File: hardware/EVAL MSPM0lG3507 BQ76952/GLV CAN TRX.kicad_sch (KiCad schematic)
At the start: 18 parts, among them Q2 2N7002, U10 MCP2542FDxMF, U5 ISO7721D, U9 LMR51603XDBVR

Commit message: boards finalized
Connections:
- net -GLV: now also C10.2, C22.2, C35.2, D11.1 (K), Q2.2 (S), R39.1, U9.2 (GND)
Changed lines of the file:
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@@
+	)
+	(junction
+		(at 127 48.26)
+		(diameter 0)
+		(color 0 0 0 0)
 	)
 	(junction
@@
 		(pts
 			(xy 69.85 91.44) (xy 69.85 93.98)
+		)
+		(stroke
+			(width 0)
+			(type default)
+		)
+	)
+	(wire
+		(pts
+			(xy 127 48.26) (xy 138.43 48.26)
 		)
 		(stroke
@@
 		(effects
 			(font
+				(size 1.27 1.27)
+			)
+			(justify left bottom)
+		)
+	)
+	(label "-GLV"
+		(at 138.43 48.26 0)
+		(effects
+			(font

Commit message: partial correctinos to kicad
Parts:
- D11: footprint LED_SMD:LED_0201_0603Metric_Pad0.64x0.40mm_HandSolder -> LED_SMD:LED_0603_1608Metric; unit x10 0.12 -> 0.118
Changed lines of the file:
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@@
 			)
 		)
-		(property "Footprint" "LED_SMD:LED_0201_0603Metric_Pad0.64x0.40mm_HandSolder"
+		(property "Footprint" "LED_SMD:LED_0603_1608Metric"
 			(at 127 34.29 0)
 			(effects
@@
 			)
 		)
-		(property "unit x10" "0.12"
+		(property "unit x10" "0.118"
 			(at 127 34.29 90)
 			(effects

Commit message: asdd
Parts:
- L4: mouser (none) -> https://www.mouser.com/ProductDetail/Bourns/SRN5040TA-101K?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; specs (none) -> 100uH, 10%, 720mA max, 560mESR, -55C, +125C; unit x10 (none) -> 0.329
- R31: value 700 -> 750; mouser (none) -> https://www.mouser.com/ProductDetail/YAGEO/RC1206JR-13750RL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; specs (none) -> 750mOhm, 250mW, 5%, 100PPM, 200C, -55C, +155C; unit x10 (none) -> 0.022
- U10: mouser (none) -> https://www.mouser.com/ProductDetail/579-MCP2542FD-E-SN; unit x10 (none) -> 0.86
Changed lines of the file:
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@@
 	(wire
 		(pts
-			(xy 53.34 76.2) (xy 53.34 93.98)
+			(xy 50.8 76.2) (xy 50.8 93.98)
 		)
 		(stroke
@@
 	(wire
 		(pts
+			(xy 50.8 76.2) (xy 48.26 76.2)
+		)
+		(stroke
+			(width 0)
+			(type default)
+		)
+	)
+	(wire
+		(pts
+			(xy 40.64 39.37) (xy 40.64 48.26)
+		)
+		(stroke
+			(width 0)
+			(type default)
+		)
+	)
+	(wire
+		(pts
+			(xy 48.26 73.66) (xy 73.66 73.66)
+		)
+		(stroke
+			(width 0)
+			(type default)
+		)
+	)
+	(wire
+		(pts
+			(xy 48.26 68.58) (xy 50.8 68.58)
+		)
+		(stroke
+			(width 0)
+			(type default)
+		)
+	)
+	(wire
+		(pts
+			(xy 104.14 35.56) (xy 104.14 48.26)
+		)
+		(stroke
+			(width 0)
+			(type default)
+		)
+	)
+	(wire
+		(pts
+			(xy 83.82 60.96) (xy 50.8 60.96)
+		)
+		(stroke
+			(width 0)
+			(type default)
+		)
+	)
+	(wire
+		(pts
+			(xy 44.45 26.67) (xy 43.18 26.67)
+		)
+		(stroke
+			(width 0)
+			(type default)
+		)
+	)
+	(wire
+		(pts
+			(xy 104.14 21.59) (xy 104.14 30.48)
+		)
+		(stroke
+			(width 0)
+			(type default)
+		)
+	)
+	(wire
+		(pts
+			(xy 25.4 27.94) (xy 27.94 27.94)
+		)
+		(stroke
+			(width 0)
+			(type default)
+		)
+	)
+	(wire
+		(pts
+			(xy 127 29.21) (xy 127 30.48)
+		)
+		(stroke
+			(width 0)
+			(type default)
+		)
+	)
+	(wire
+		(pts
+			(xy 69.85 91.44) (xy 69.85 93.98)
+		)
+		(stroke
+			(width 0)
+			(type default)
+		)
+	)
+	(wire
+		(pts
+			(xy 127 48.26) (xy 138.43 48.26)
+		)
+		(stroke
+			(width 0)
+			(type default)
+		)
+	)
+	(wire
+		(pts
+			(xy 68.58 29.21) (xy 92.71 29.21)
+		)
+		(stroke
+			(width 0)
+			(type default)
+		)
+	)
+	(wire
+		(pts
+			(xy 50.8 93.98) (xy 60.96 93.98)
+		)
+		(stroke
+			(width 0)
+			(type default)
+		)
+	)
+	(wire
+		(pts
+			(xy 60.96 71.12) (xy 73.66 71.12)
+		)
+		(stroke
+			(width 0)
+			(type default)
+		)
+	)
+	(wire
+		(pts
+			(xy 109.22 21.59) (xy 104.14 21.59)
+		)
+		(stroke
+			(width 0)
+			(type default)
+		)
+	)
+	(wire
+		(pts
+			(xy 68.58 26.67) (xy 76.2 26.67)
+		)
+		(stroke
+			(width 0)
+			(type default)
+		)
+	)
+	(wire
+		(pts
+			(xy 34.29 24.13) (xy 34.29 40.64)
+		)
+		(stroke
+			(width 0)
+			(type default)
+		)
+	)
+	(wire
+		(pts
+			(xy 92.71 39.37) (xy 92.71 38.1)
+		)
+		(stroke
+			(width 0)
+			(type default)
+		)
+	)
+	(wire
+		(pts
+			(xy 76.2 21.59) (xy 74.93 21.59)
+		)
+		(stroke
+			(width 0)
+			(type default)
+		)
+	)
+	(wire
+		(pts
 			(xy 48.26 71.12) (xy 60.96 71.12)
 		)
@@
 	(wire
 		(pts
-			(xy 53.34 76.2) (xy 48.26 76.2)
-		)
-		(stroke
-			(width 0)
-			(type default)
-		)
-	)
-	(wire
-		(pts
-			(xy 40.64 39.37) (xy 40.64 48.26)
-		)
-		(stroke
-			(width 0)
-			(type default)
-		)
-	)
-	(wire
-		(pts
-			(xy 48.26 73.66) (xy 73.66 73.66)
-		)
-		(stroke
-			(width 0)
-			(type default)
-		)
-	)
-	(wire
-		(pts
-			(xy 48.26 68.58) (xy 53.34 68.58)
-		)
-		(stroke
-			(width 0)
-			(type default)
-		)
-	)
-	(wire
-		(pts
-			(xy 104.14 35.56) (xy 104.14 48.26)
-		)
-		(stroke
-			(width 0)
-			(type default)
-		)
-	)
-	(wire
-		(pts
-			(xy 83.82 60.96) (xy 53.34 60.96)
-		)
-		(stroke
-			(width 0)
-			(type default)
-		)
-	)
-	(wire
-		(pts
-			(xy 44.45 26.67) (xy 43.18 26.67)
-		)
-		(stroke
-			(width 0)
-			(type default)
-		)
-	)
-	(wire
-		(pts
-			(xy 104.14 21.59) (xy 104.14 30.48)
-		)
-		(stroke
-			(width 0)
-			(type default)
-		)
-	)
-	(wire
-		(pts
-			(xy 25.4 27.94) (xy 27.94 27.94)
-		)
-		(stroke
-			(width 0)
-			(type default)
-		)
-	)
-	(wire
-		(pts
-			(xy 127 29.21) (xy 127 30.48)
-		)
-		(stroke
-			(width 0)
-			(type default)
-		)
-	)
-	(wire
-		(pts
-			(xy 69.85 91.44) (xy 69.85 93.98)
-		)
-		(stroke
-			(width 0)
-			(type default)
-		)
-	)
-	(wire
-		(pts
-			(xy 127 48.26) (xy 138.43 48.26)
-		)
-		(stroke
-			(width 0)
-			(type default)
-		)
-	)
-	(wire
-		(pts
-			(xy 68.58 29.21) (xy 92.71 29.21)
-		)
-		(stroke
-			(width 0)
-			(type default)
-		)
-	)
-	(wire
-		(pts
-			(xy 53.34 93.98) (xy 60.96 93.98)
-		)
-		(stroke
-			(width 0)
-			(type default)
-		)
-	)
-	(wire
-		(pts
-			(xy 60.96 71.12) (xy 73.66 71.12)
-		)
-		(stroke
-			(width 0)
-			(type default)
-		)
-	)
-	(wire
-		(pts
-			(xy 109.22 21.59) (xy 104.14 21.59)
-		)
-		(stroke
-			(width 0)
-			(type default)
-		)
-	)
-	(wire
-		(pts
-			(xy 68.58 26.67) (xy 76.2 26.67)
-		)
-		(stroke
-			(width 0)
-			(type default)
-		)
-	)
-	(wire
-		(pts
-			(xy 34.29 24.13) (xy 34.29 40.64)
-		)
-		(stroke
-			(width 0)
-			(type default)
-		)
-	)
-	(wire
-		(pts
-			(xy 92.71 39.37) (xy 92.71 38.1)
-		)
-		(stroke
-			(width 0)
-			(type default)
-		)
-	)
-	(wire
-		(pts
-			(xy 76.2 21.59) (xy 74.93 21.59)
-		)
-		(stroke
-			(width 0)
-			(type default)
-		)
-	)
-	(wire
-		(pts
 			(xy 69.85 93.98) (xy 60.96 93.98)
 		)
@@
 	(wire
 		(pts
-			(xy 53.34 60.96) (xy 53.34 68.58)
+			(xy 50.8 60.96) (xy 50.8 68.58)
 		)
 		(stroke
@@
 			)
 		)
-		(property "mouser" ""
+		(property "mouser" "https://www.mouser.com/ProductDetail/Bourns/SRN5040TA-101K?qs=qSfuJ%252Bfl%2Fd6IGmzq6oDX8Q%3D%3D"
 			(at 81.28 21.59 90)
 			(effects
@@
 			)
 		)
-		(property "specs" ""
+		(property "specs" "100uH, 10%, 720mA max, 560mESR, -55C, +125C"
+			(at 81.28 21.59 90)
+			(effects
+				(font
+					(size 1.27 1.27)
+				)
+				(hide yes)
+			)
+		)
+		(property "unit x10" "0.329"
 			(at 81.28 21.59 90)
 			(effects
@@
 			)
 		)
+		(property "mouser" "https://www.mouser.com/ProductDetail/579-MCP2542FD-E-SN"
+			(at 86.36 76.2 0)
+			(effects
+				(font
+					(size 1.27 1.27)
+				)
+				(hide yes)
+			)
+		)
+		(property "unit x10" "0.86"
+			(at 86.36 76.2 0)
+			(effects
+				(font
+					(size 1.27 1.27)
+				)
+				(hide yes)
+			)
+		)
 		(pin "7"
 		)
@@
 			)
 		)
-		(property "Value" "700"
+		(property "Value" "750"
 			(at 129.032 26.67 0)
 			(effects
@@
 			(at 127 25.4 0)
 			(effects
+				(font
+					(size 1.27 1.27)
+				)
+				(hide yes)
+			)
+		)
+		(property "mouser" "https://www.mouser.com/ProductDetail/YAGEO/RC1206JR-13750RL?qs=sGAEpiMZZMvdGkrng054t8AJgcdMkx7xRBGyMWDk%2FFM%3D"
+			(at 127 25.4 0)
+			(effects
+				(font
+					(size 1.27 1.27)
+				)
+				(hide yes)
+			)
+		)
+		(property "specs" "750mOhm, 250mW, 5%, 100PPM, 200C, -55C, +155C"
+			(at 127 25.4 0)
+			(effects
+				(font
+					(size 1.27 1.27)
+				)
+				(hide yes)
+			)
+		)
+		(property "unit x10" "0.022"
+			(at 127 25.4 0)
+			(effects

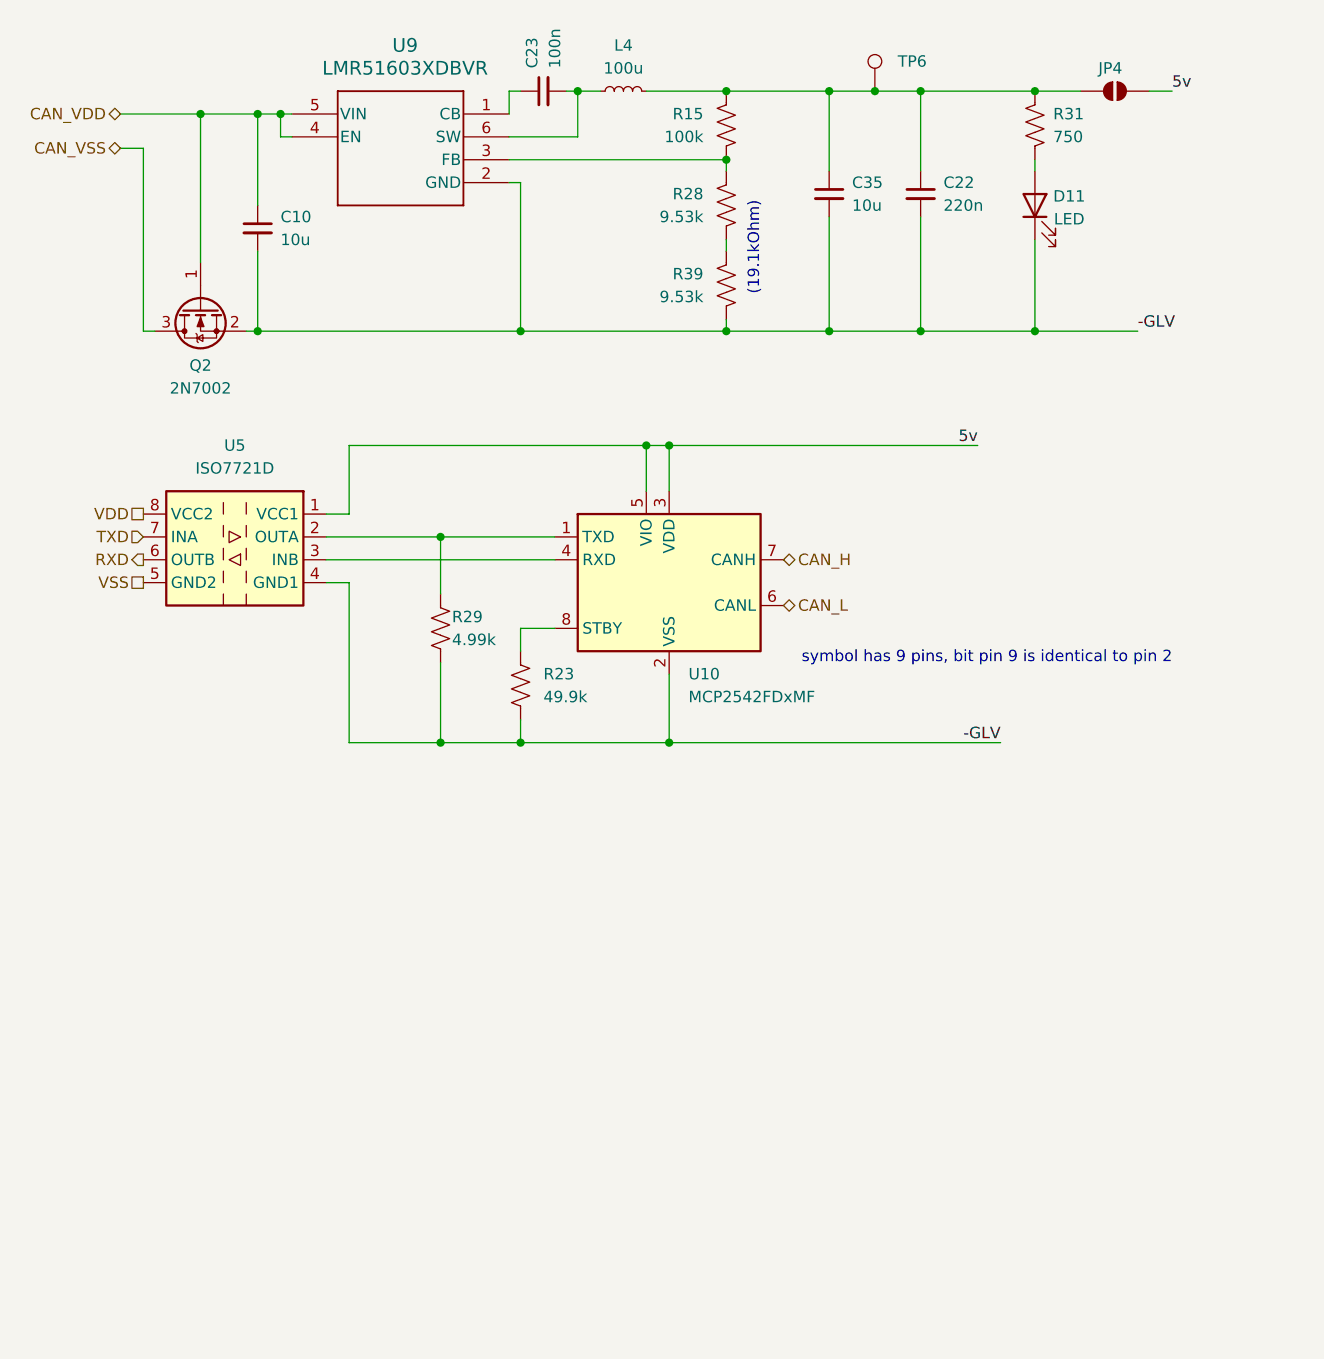
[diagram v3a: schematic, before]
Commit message: corrected CAN transceiver parts
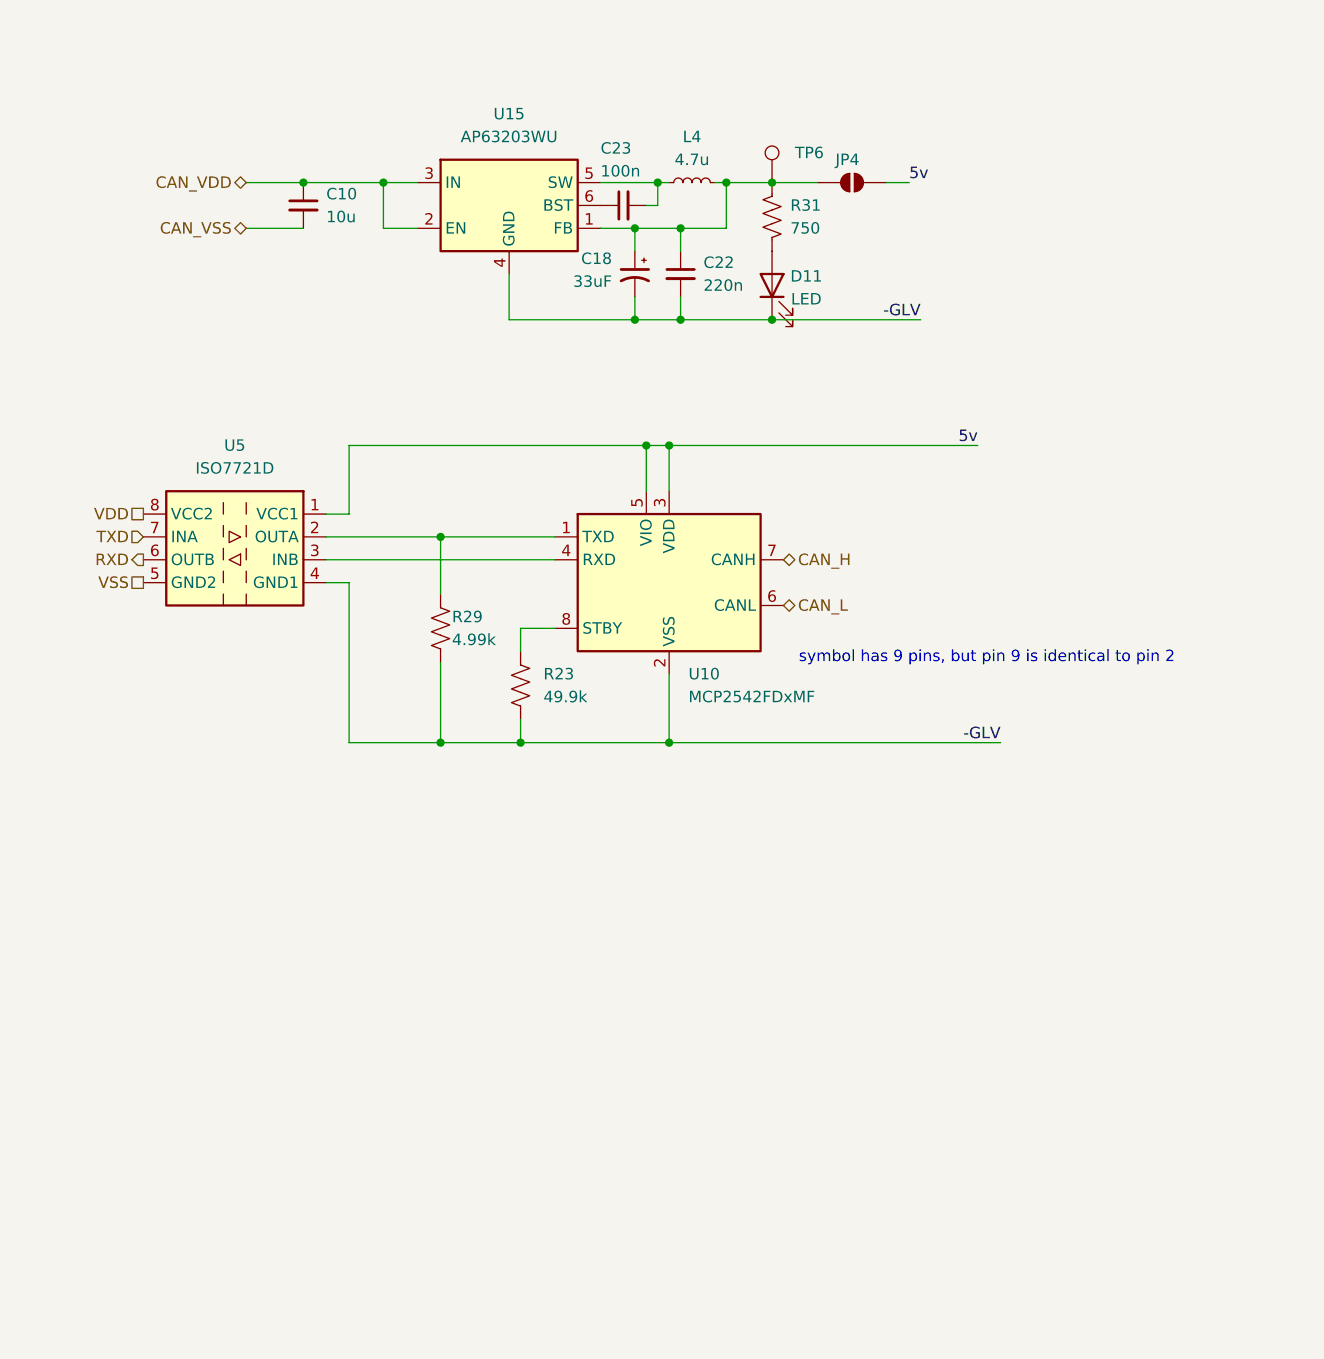
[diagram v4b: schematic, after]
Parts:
- removed C35: 10u, Capacitor_SMD:C_1206_3216Metric_Pad1.33x1.80mm_HandSolder, symbol Device:C_Small
- removed Q2: 2N7002, Package_TO_SOT_SMD:SOT-23, symbol Transistor_FET:2N7002
- removed R15: 100k, Resistor_SMD:R_1206_3216Metric_Pad1.30x1.75mm_HandSolder, symbol Device:R_US
- removed R28, R39: 9.53k, Resistor_SMD:R_1206_3216Metric_Pad1.30x1.75mm_HandSolder, symbol Device:R_US
- removed U9: LMR51603XDBVR, zzLocalLibraries-Footprints:DBV0006A-MFG-IPC_B, symbol zzLocalLibrary:LMR51603XDBVR
- added C18: 33uF, Diode_SMD:D_1206_3216Metric_Pad1.42x1.75mm_HandSolder, symbol Device:C_Polarized_Small_US
- added U15: AP63203WU, Package_TO_SOT_SMD:TSOT-23-6, symbol Regulator_Switching:AP63203WU
- L4: value 100u -> 4.7u; footprint Inductor_SMD:L_TDK_VLS6045EX_VLS6045AF -> Inductor_SMD:L_0805_2012Metric_Pad1.05x1.20mm_HandSolder; mouser https://www.mouser.com/ProductDetail/Bourns/SRN5040TA-101K?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 -> https://www.mouser.com/ProductDetail/TDK/MLZ2012N4R7LTD25?q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; specs 100uH, 10%, 720mA max, 560mESR, -55C, +125C -> 4.7uH; unit x10 0.329 -> 0.091
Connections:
- net -GLV: now also C18.2, U15.4 (GND); no longer C10.2
- net CAN_VDD: now also U15.2 (EN), U15.3 (IN)
- net CAN_VSS: now also C10.2
- net at C23.2, L4.1: now also U15.5 (SW)
- net at C22.1, JP4.1 (A), L4.2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: now also C18.1, U15.1 (FB)
- net at C23.1: now also U15.6 (BST)
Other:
- note added: "symbol has 9 pins, but pin 9 is identical to pin 2"
- note removed: "(19.1kOhm)"
- note removed: "symbol has 9 pins, bit pin 9 is identical to pin 2"
- moved on the sheet: C10, C23, D11, JP4, L4, R31, TP6

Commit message: bluhhh
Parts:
- removed C18: 33uF, Diode_SMD:D_1206_3216Metric_Pad1.42x1.75mm_HandSolder, symbol Device:C_Polarized_Small_US
- added C18: 10u, Capacitor_SMD:C_1206_3216Metric_Pad1.33x1.80mm_HandSolder, symbol Device:C_Small
- C22: value 220n -> 10u; mouser https://www.mouser.com/ProductDetail/Samsung-Electro-Mechanics/CL31B224KBFNNNF?qs=sGAEpiMZZMsh%252B1woXyUXj7iNKXiFkBmw7C%252BUlKpuDJ8%3D -> https://www.mouser.com/ProductDetail/Samsung-Electro-Mechanics/CL31A106KBHNNNE?qs=sGAEpiMZZMsh%252B1woXyUXjxqcB7t9naYpzWmpMbMJIKQ%3D; specs 50VDC, X7R, 10%, -55C, +125C, 220nF -> 10uF, 50VDC, X5R, 10%, -55C, +85C; unit x10 0.05 -> 0.07
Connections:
- net -GLV is gone; now on net CAN_VSS: C22.2, D11.1 (K), R23.1, R29.2, U10.2 (VSS), U10.9 (VSS), U15.4 (GND), U5.4 (GND1)
- net CAN_VSS: now also C18.2
- net at C22.1, JP4.1 (A), L4.2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: now also C18.1
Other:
- moved on the sheet: C10, D11, JP4, R31, TP6

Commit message: ac;lkacnl;
acea;kca
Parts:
- removed C18: 10u, Capacitor_SMD:C_1206_3216Metric_Pad1.33x1.80mm_HandSolder, symbol Device:C_Small
- removed C23: 100n, Capacitor_SMD:C_1206_3216Metric_Pad1.33x1.80mm_HandSolder, symbol Device:C_Small
- removed L4: 4.7u, Inductor_SMD:L_0805_2012Metric_Pad1.05x1.20mm_HandSolder, symbol Device:L_Small
- removed U15: AP63203WU, Package_TO_SOT_SMD:TSOT-23-6, symbol Regulator_Switching:AP63203WU
- added U8: L78L05_SOT89, Package_TO_SOT_SMD:SOT-89-3, symbol Regulator_Linear:L78L05_SOT89
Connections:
- net CAN_VDD: now also U8.3 (IN)
- net CAN_VSS: now also U8.2 (GND)
- net at C22.1, JP4.1 (A), R31.1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: now also U8.1 (OUT)
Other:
- moved on the sheet: C10, C22, D11, JP4, R31, TP6
